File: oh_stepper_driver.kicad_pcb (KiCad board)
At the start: 2 copper layers, 61 x 43.2 mm, 45 parts, among them P1 CONN_01X04, P2 CONN_01X02, P3 CONN_01X02, Q1 CSD18531Q5A, Q2 CSD18531Q5A, Q3 CSD18531Q5A, Q4 CSD18531Q5A, Q5 CSD18531Q5A, Q6 CSD18531Q5A, Q7 CSD18531Q5A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

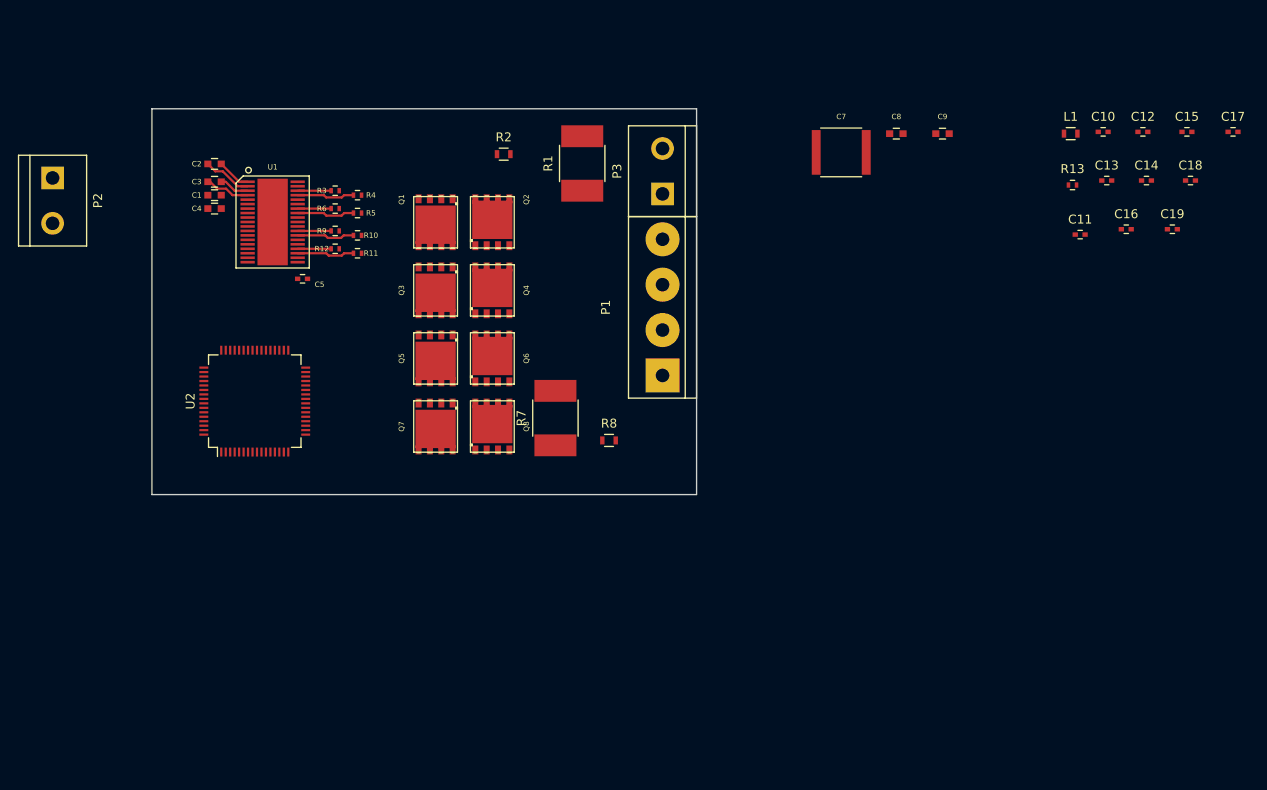
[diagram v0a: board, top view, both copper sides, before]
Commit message: routing FETs
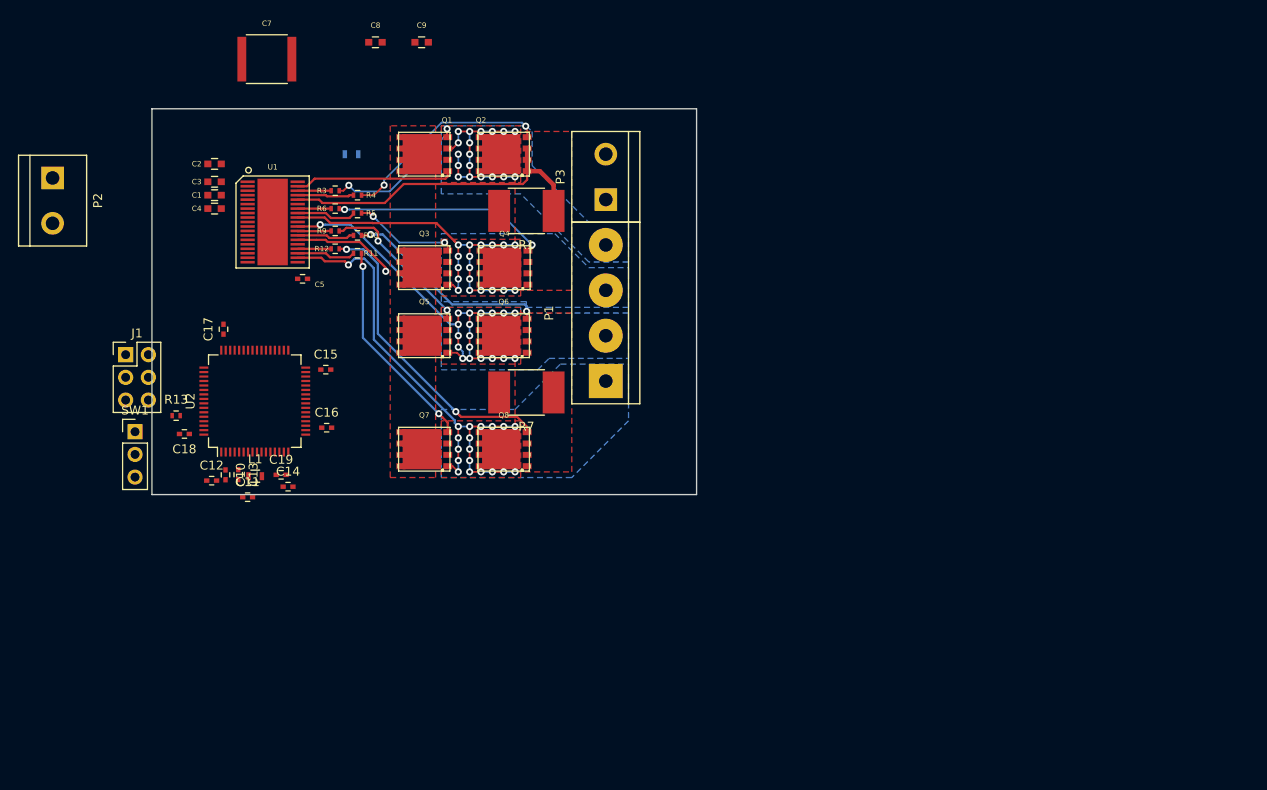
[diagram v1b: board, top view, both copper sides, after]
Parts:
- added J1: JTAG, Pin_Headers:Pin_Header_Straight_2x03_Pitch2.54mm, F.Cu at (113.9, 83.4)
- added SW1: BOOT_MODE, Pin_Headers:Pin_Header_Straight_1x03_Pitch2.54mm, F.Cu at (115.0, 92.0)
- R2, R8: moved to B.Cu
- moved C18 116.1 mm to (120.5, 92.3), turned to 180 degrees
- moved C17 115.1 mm to (124.8, 80.5), turned to 90 degrees
- moved C12 111.3 mm to (123.5, 97.5)
- moved C10 105.5 mm to (125.1, 96.8), turned to 270 degrees
- moved R13 103.6 mm to (119.5, 90.2)
- moved C19 103.5 mm to (131.3, 96.8)
- moved C13 102.6 mm to (126.5, 96.8), turned to 270 degrees
- moved C14 102.0 mm to (132.1, 98.2)
- moved C15 100.0 mm to (136.3, 85.1)
- moved L1 99.0 mm to (128.4, 97.0)
- moved C11 97.7 mm to (127.5, 99.3)
- moved C16 92.2 mm to (136.4, 91.6)
- moved C7 65.1 mm to (129.7, 50.3)
- moved C8 59.2 mm to (141.9, 48.4)
- moved C9 59.2 mm to (147.0, 48.4)
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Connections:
- C12 pad 1: (no net) -> +3V3
- C12 pad 2: (no net) -> GND
- C14 pad 1: (no net) -> +3.3VADC
- C14 pad 2: (no net) -> GNDA
- R13 pad 2: (no net) -> Net-(R13-Pad2)
- U2 pad 10: (no net) -> Net-(U2-Pad10)
- U2 pad 11: (no net) -> Net-(U2-Pad11)
- U2 pad 14: (no net) -> Net-(U2-Pad14)
- U2 pad 15: (no net) -> Net-(U2-Pad15)
- U2 pad 16: (no net) -> Net-(U2-Pad16)
- U2 pad 17: (no net) -> Net-(U2-Pad17)
- U2 pad 2: (no net) -> Net-(U2-Pad2)
- U2 pad 20: (no net) -> Net-(U2-Pad20)
- U2 pad 24: (no net) -> Net-(U2-Pad24)
- U2 pad 25: (no net) -> Net-(U2-Pad25)
- U2 pad 26: (no net) -> Net-(U2-Pad26)
- U2 pad 27: (no net) -> Net-(U2-Pad27)
- U2 pad 28: (no net) -> Net-(U2-Pad28)
- U2 pad 29: (no net) -> Net-(U2-Pad29)
- U2 pad 3: (no net) -> Net-(U2-Pad3)
- U2 pad 30: (no net) -> Net-(U2-Pad30)
- U2 pad 33: (no net) -> Net-(U2-Pad33)
- U2 pad 34: (no net) -> Net-(U2-Pad34)
- U2 pad 35: (no net) -> Net-(U2-Pad35)
- U2 pad 36: (no net) -> Net-(U2-Pad36)
- U2 pad 37: (no net) -> Net-(U2-Pad37)
- U2 pad 38: (no net) -> Net-(U2-Pad38)
- U2 pad 39: (no net) -> Net-(U2-Pad39)
- U2 pad 4: (no net) -> Net-(U2-Pad4)
- U2 pad 40: (no net) -> Net-(U2-Pad40)
- U2 pad 46: (no net) -> /JTMS
- U2 pad 49: (no net) -> /JTCK
- U2 pad 50: (no net) -> /JTDI
- U2 pad 55: (no net) -> /JTDO
- U2 pad 56: (no net) -> /NJTRST
- U2 pad 57: (no net) -> Net-(U2-Pad57)
- U2 pad 58: (no net) -> Net-(U2-Pad58)
- U2 pad 59: (no net) -> Net-(U2-Pad59)
- U2 pad 61: (no net) -> Net-(U2-Pad61)
- U2 pad 62: (no net) -> Net-(U2-Pad62)
- U2 pad 8: (no net) -> Net-(U2-Pad8)
- U2 pad 9: (no net) -> Net-(U2-Pad9)
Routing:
- net /DRV8711/BOUT2: track 0.00 -> 54.3 mm, vias 0 -> 19
- net /DRV8711/BOUT1: track 0.00 -> 46.4 mm, vias 0 -> 19
- net /DRV8711/AOUT2: track 0.00 -> 42.7 mm, vias 0 -> 18
- net /DRV8711/AOUT1: track 0.00 -> 40.9 mm, vias 0 -> 18
- net /DRV8711/AISENP: track 0.00 -> 36.9 mm
- net Net-(Q8-PadG): track 0.00 -> 34.5 mm, vias 0 -> 2
- net Net-(Q4-PadG): track 0.00 -> 24.1 mm, vias 0 -> 2
- net Net-(Q7-PadG): track 0.00 -> 24.0 mm, vias 0 -> 2
- net Net-(Q2-PadG): track 0.00 -> 23.5 mm, vias 0 -> 2
- net Net-(Q6-PadG): track 0.00 -> 23.3 mm, vias 0 -> 2
- net Net-(Q5-PadG): track 0.00 -> 17.6 mm, vias 0 -> 2
- net Net-(Q1-PadG): track 0.06 -> 16.8 mm, vias 0 -> 2
- net Net-(Q3-PadG): track 0.00 -> 12.1 mm, vias 0 -> 2
- net /DRV8711/BISENP: track 0.00 -> 11.5 mm, vias 0 -> 1
- net Net-(C3-Pad2): track 5.49 -> 0.00 mm
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- added copper zone on F.Cu, net /DRV8711/AISENP
- added copper zone on B.Cu, net /DRV8711/AOUT1
- added copper zone on F.Cu, net /DRV8711/AOUT1
- added copper zone on B.Cu, net /DRV8711/AOUT2
- added copper zone on F.Cu, net /DRV8711/AOUT2
- added copper zone on F.Cu, net /DRV8711/BISENP
- added copper zone on B.Cu, net /DRV8711/BOUT1
- added copper zone on F.Cu, net /DRV8711/BOUT1
- added copper zone on B.Cu, net /DRV8711/BOUT2
- added copper zone on F.Cu, net /DRV8711/BOUT2
- added copper zone on F.Cu, net VM

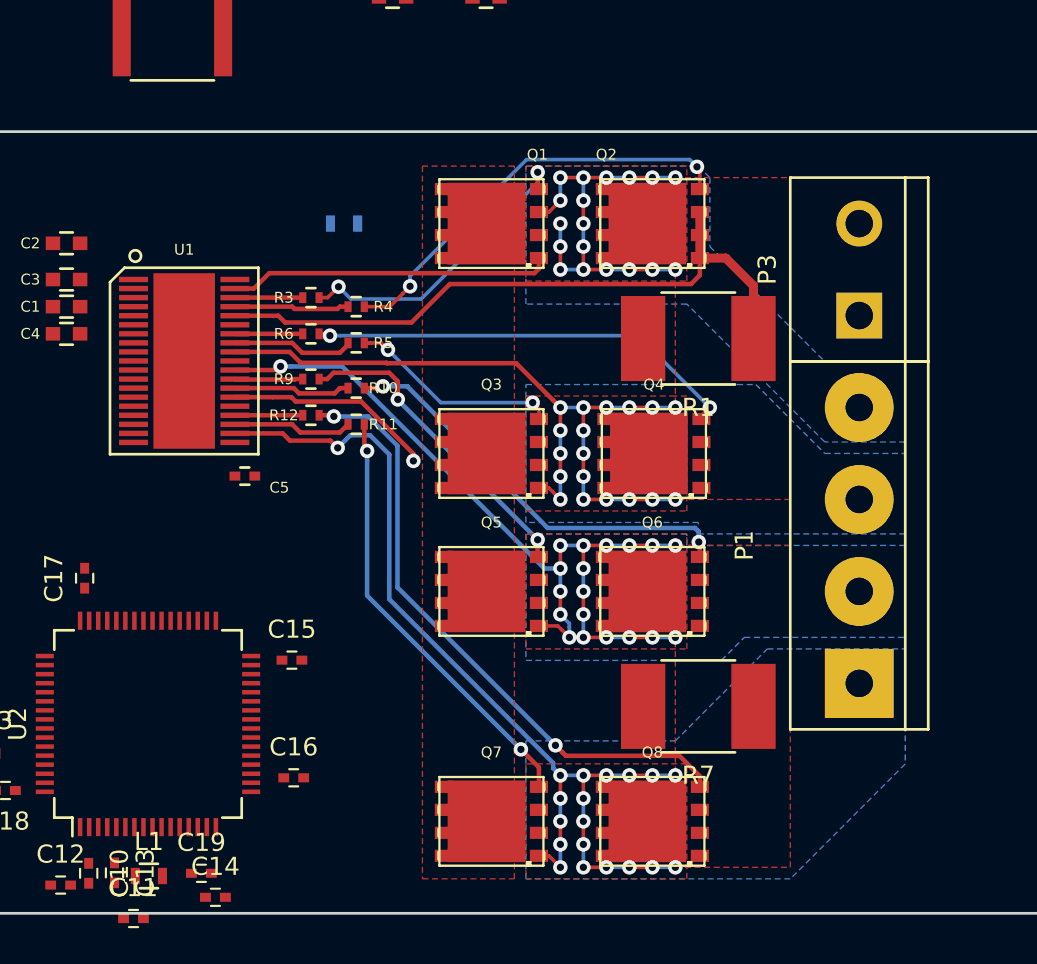
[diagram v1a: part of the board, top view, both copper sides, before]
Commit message: 4 layers
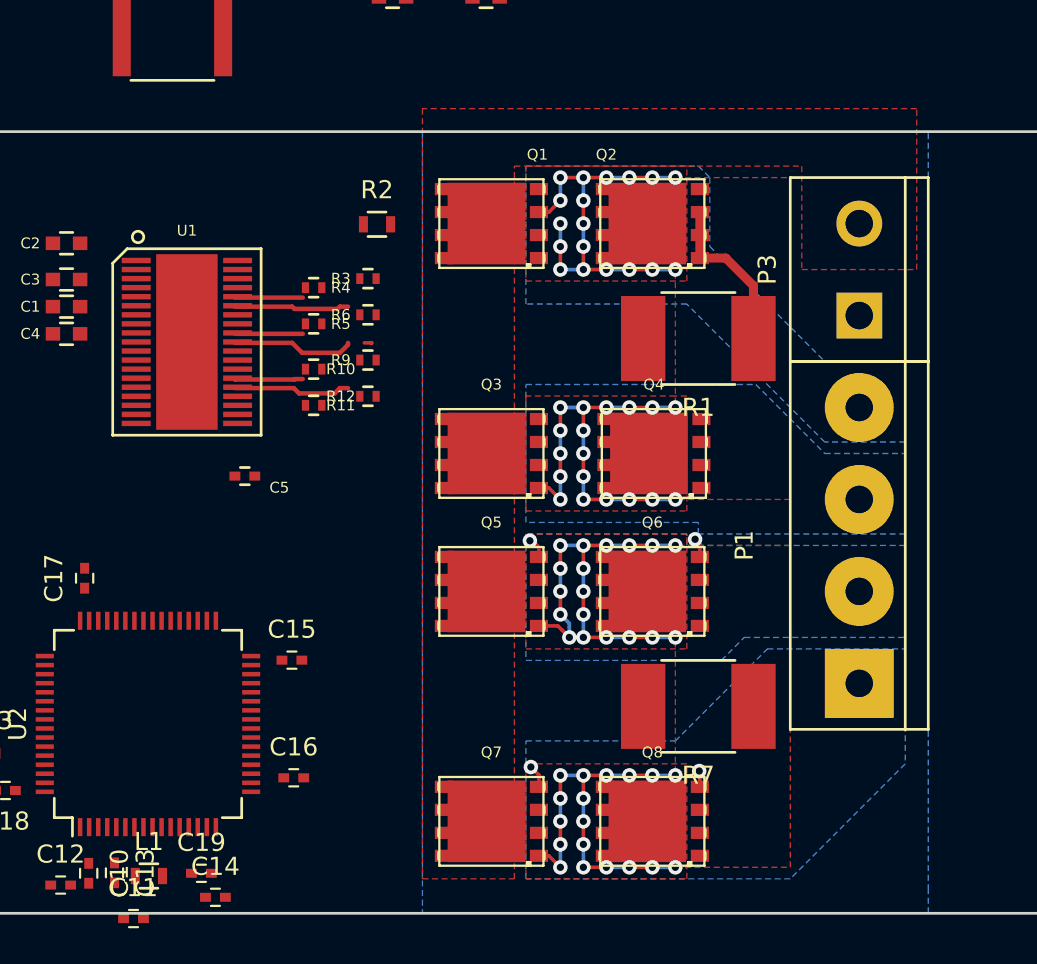
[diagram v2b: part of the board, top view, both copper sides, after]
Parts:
- R2: moved to F.Cu
- moved R12 3.32 mm to (140.5, 70.5)
- moved R3 3.32 mm to (140.5, 64.0)
- moved R6 3.32 mm to (140.5, 66.0)
- moved R9 3.32 mm to (140.5, 68.5)
- moved R10 2.57 mm to (137.5, 69.0)
- moved R11 2.57 mm to (137.5, 71.0)
- moved R4 2.57 mm to (137.5, 64.5)
- moved R5 2.57 mm to (137.5, 66.5)
- moved R2 1.82 mm to (141.0, 61.0)
- moved U1 1.06 mm to (130.5, 67.5)
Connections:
- P2 pad 1: VM -> GND
- P2 pad 2: GND -> VM
- P3 pad 1: VM -> GND
- P3 pad 2: GND -> VM
- U2 pad 10: Net-(U2-Pad10) -> (no net)
- U2 pad 11: Net-(U2-Pad11) -> (no net)
- U2 pad 14: Net-(U2-Pad14) -> (no net)
- U2 pad 15: Net-(U2-Pad15) -> (no net)
- U2 pad 16: Net-(U2-Pad16) -> (no net)
- U2 pad 17: Net-(U2-Pad17) -> (no net)
- U2 pad 2: Net-(U2-Pad2) -> (no net)
- U2 pad 20: Net-(U2-Pad20) -> (no net)
- U2 pad 24: Net-(U2-Pad24) -> (no net)
- U2 pad 25: Net-(U2-Pad25) -> (no net)
- U2 pad 26: Net-(U2-Pad26) -> (no net)
- U2 pad 27: Net-(U2-Pad27) -> (no net)
- U2 pad 28: Net-(U2-Pad28) -> (no net)
- U2 pad 29: Net-(U2-Pad29) -> (no net)
- U2 pad 3: Net-(U2-Pad3) -> (no net)
- U2 pad 30: Net-(U2-Pad30) -> (no net)
- U2 pad 33: Net-(U2-Pad33) -> (no net)
- U2 pad 34: Net-(U2-Pad34) -> (no net)
- U2 pad 35: Net-(U2-Pad35) -> (no net)
- U2 pad 36: Net-(U2-Pad36) -> (no net)
- U2 pad 37: Net-(U2-Pad37) -> (no net)
- U2 pad 38: Net-(U2-Pad38) -> (no net)
- U2 pad 39: Net-(U2-Pad39) -> (no net)
- U2 pad 4: Net-(U2-Pad4) -> (no net)
- U2 pad 40: Net-(U2-Pad40) -> (no net)
- U2 pad 57: Net-(U2-Pad57) -> (no net)
- U2 pad 58: Net-(U2-Pad58) -> (no net)
- U2 pad 59: Net-(U2-Pad59) -> (no net)
- U2 pad 61: Net-(U2-Pad61) -> (no net)
- U2 pad 62: Net-(U2-Pad62) -> (no net)
- U2 pad 8: Net-(U2-Pad8) -> (no net)
- U2 pad 9: Net-(U2-Pad9) -> (no net)
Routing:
- net /DRV8711/AISENP: track 36.9 -> 12.8 mm
- net Net-(Q4-PadG): track 24.1 -> 0.17 mm, vias 2 -> 0
- net Net-(Q2-PadG): track 23.5 -> 0.00 mm, vias 2 -> 0
- net /DRV8711/AOUT1: track 40.9 -> 23.0 mm
- net /DRV8711/BOUT1: track 46.4 -> 29.1 mm, vias 19 -> 18
- net Net-(Q1-PadG): track 16.8 -> 0.10 mm, vias 2 -> 0
- net /DRV8711/AOUT2: track 42.7 -> 27.2 mm
- net /DRV8711/BOUT2: track 54.3 -> 42.0 mm, vias 19 -> 18
- net Net-(Q3-PadG): track 12.1 -> 0.00 mm, vias 2 -> 0
- net Net-(Q8-PadG): track 34.5 -> 25.9 mm, vias 2 -> 1
- net /DRV8711/BISENP: track 11.5 -> 3.80 mm, vias 1 -> 0
- net Net-(Q5-PadG): track 17.6 -> 10.00 mm, vias 2 -> 1
- net GND: track 0.00 -> 6.76 mm
- net /DRV8711/A2HS: track 6.76 -> 0.00 mm
- net /DRV8711/B2HS: track 6.62 -> 0.00 mm
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- added copper zone on In1.Cu, net /DRV8711/AOUT1
- added copper zone on In2.Cu, net /DRV8711/AOUT1
- added copper zone on In1.Cu, net /DRV8711/AOUT2
- added copper zone on In2.Cu, net /DRV8711/AOUT2
- added copper zone on In1.Cu, net /DRV8711/BOUT1
- added copper zone on In2.Cu, net /DRV8711/BOUT1
- added copper zone on In1.Cu, net /DRV8711/BOUT2
- added copper zone on In2.Cu, net /DRV8711/BOUT2
- added copper zone on B.Cu, net GND
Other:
- copper layers 2 -> 4

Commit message: routing control signals
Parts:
- R8: moved to F.Cu
- moved R8 10.7 mm to (137.7, 74.0)
- moved R2 4.00 mm to (137.0, 61.0)
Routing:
- net /DRV8711/BISENP: track 3.80 -> 60.1 mm, vias 0 -> 2
- net /DRV8711/AOUT1: track 23.0 -> 50.9 mm, vias 18 -> 19
- net Net-(Q2-PadG): track 0.00 -> 25.4 mm, vias 0 -> 2
- net GND: track 6.76 -> 32.0 mm, vias 0 -> 16
- net /DRV8711/AISENP: track 12.8 -> 37.9 mm, vias 0 -> 2
- net Net-(Q4-PadG): track 0.17 -> 21.2 mm, vias 0 -> 2
- net /DRV8711/AOUT2: track 27.2 -> 47.5 mm, vias 18 -> 19
- net /DRV8711/BOUT1: track 29.1 -> 47.3 mm, vias 18 -> 19
- net Net-(Q3-PadG): track 0.00 -> 14.9 mm, vias 0 -> 2
- net Net-(Q1-PadG): track 0.10 -> 13.5 mm, vias 0 -> 2
- net /DRV8711/BOUT2: track 42.0 -> 53.5 mm, vias 18 -> 19
- net /DRV8711/B2LS: track 0.00 -> 7.64 mm
- net /DRV8711/A1HS: track 0.00 -> 7.49 mm
- net Net-(Q7-PadG): track 18.9 -> 26.2 mm, vias 1 -> 2
- net /DRV8711/B1HS: track 0.00 -> 7.26 mm
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- added copper zone on F.Cu, net GND
- added copper zone on In2.Cu, net GND

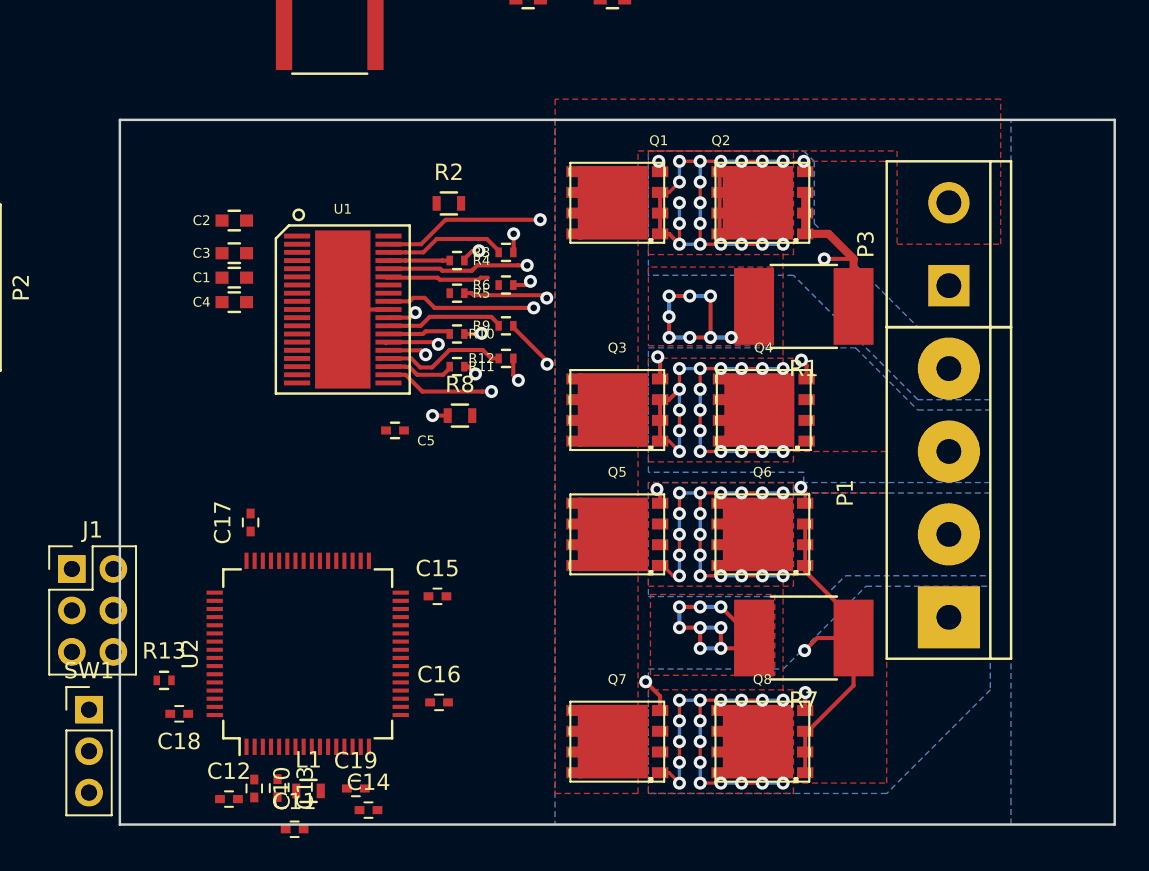
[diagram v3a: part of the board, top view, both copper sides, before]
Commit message: cooper pour for motor driver
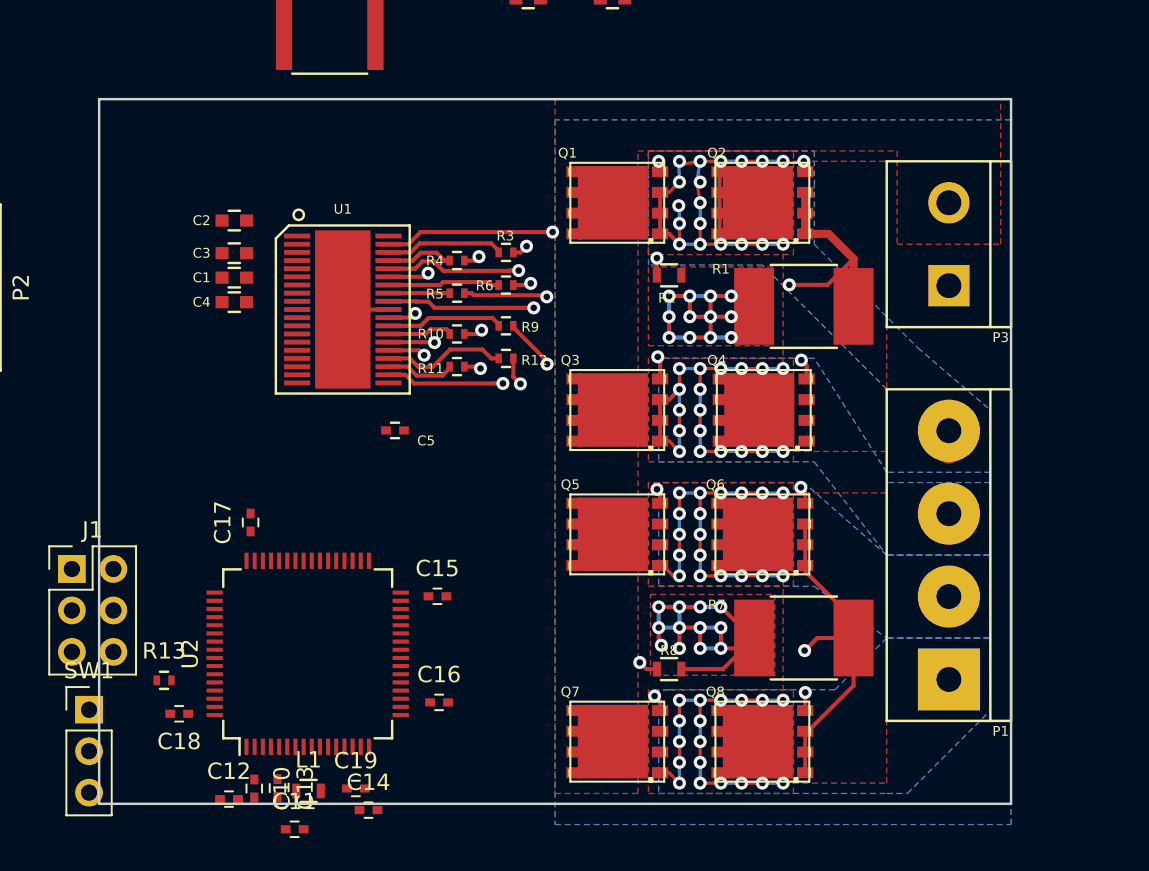
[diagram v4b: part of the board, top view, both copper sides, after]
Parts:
- moved R8 20.1 mm to (150.5, 89.5)
- moved R2 14.2 mm to (150.5, 65.4)
- moved P1 3.81 mm to (167.6, 82.5)
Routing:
- net /DRV8711/BISENN: track 7.23 -> 30.9 mm
- net GND: track 32.0 -> 48.5 mm, vias 16 -> 24
- net /DRV8711/AISENN: track 6.35 -> 18.0 mm, vias 0 -> 2
- net /DRV8711/A2LS: track 0.00 -> 6.90 mm
- net /DRV8711/A2HS: track 0.00 -> 3.75 mm
- net Net-(Q8-PadG): track 32.7 -> 34.5 mm
- net /DRV8711/BOUT2: track 53.5 -> 55.2 mm
- net Net-(Q5-PadG): track 16.0 -> 14.7 mm
- net Net-(Q1-PadG): track 13.5 -> 12.3 mm
- net Net-(Q7-PadG): track 26.2 -> 27.3 mm
- net /DRV8711/AISENP: track 37.9 -> 39.0 mm
- net /DRV8711/BOUT1: track 47.3 -> 46.4 mm
- net Net-(Q6-PadG): track 27.1 -> 26.2 mm
- net Net-(Q4-PadG): track 21.2 -> 22.0 mm
- net /DRV8711/BISENP: track 60.1 -> 60.8 mm
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- added copper zone on In1.Cu, net VM
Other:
- board size 61 x 43.2 mm -> 55.9 x 43.2 mm
